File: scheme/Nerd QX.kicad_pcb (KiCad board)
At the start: 6 copper layers, 89 x 184 mm, 263 parts, among them J1 Connector 02x01, J2 Conn_01x04, M1 Fan_4pin, M2 Fan_4pin, M3 Fan_4pin, U10 CSD95472Q5MC, U19 BM1370_mode1, U2 TMUX1109RSVR, U20 BM1370_mode1, U25 BM1370_mode1, U26 BM1370_mode1, U3 TPS53647, U30 T-Display-S3, U32 EMC2302-1, U33 TXU0102-DCU, U35 TXU0304PW, U36 MCP1824T-1202E, U37 TMP1075, U38 TMP1075, U4 CSD95472Q5MC, U5 TMP451, U6 AP3211, U7 MCP1824T-0802E, U8 25MHz, U9 CSD95472Q5MC

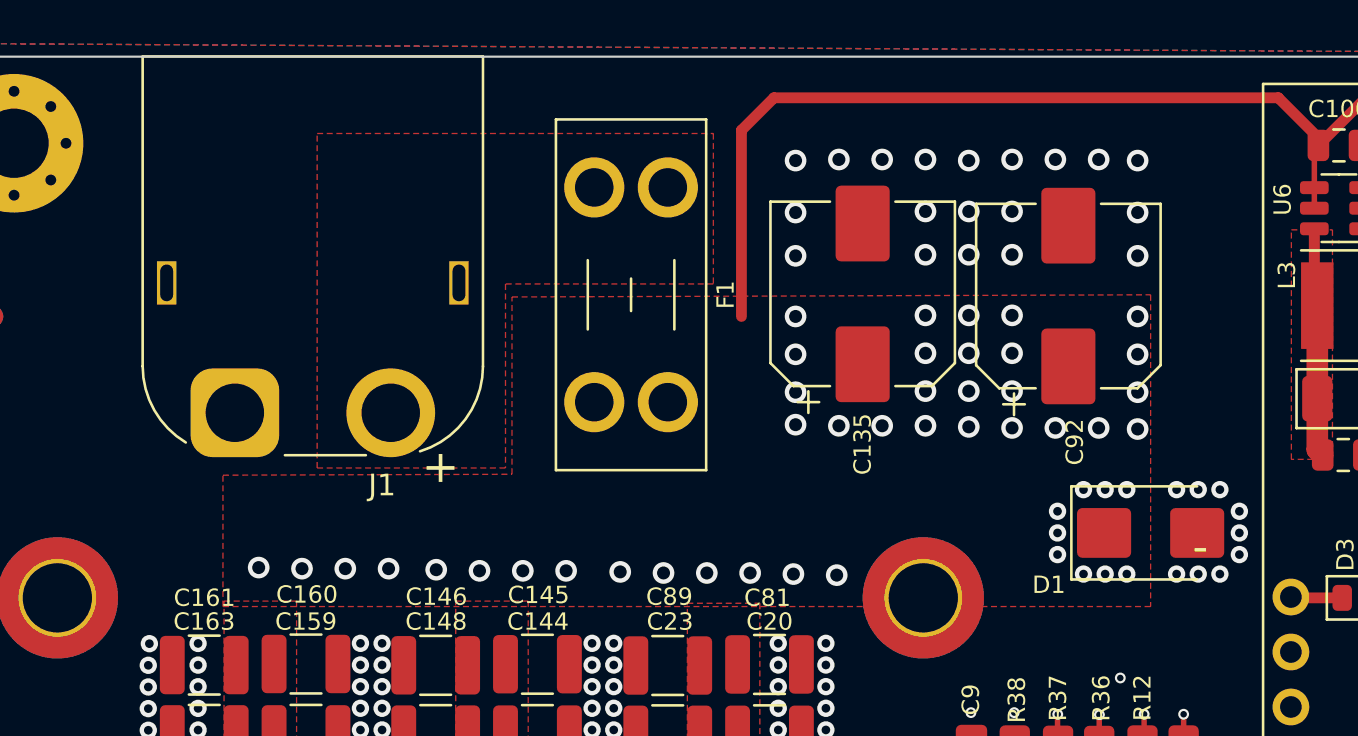
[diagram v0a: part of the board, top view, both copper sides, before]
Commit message: Moved J1 XT60 connector from top to bottom side of the board. Exported new gerber files, drill files and P&P files. Exported new PCB STEP file.
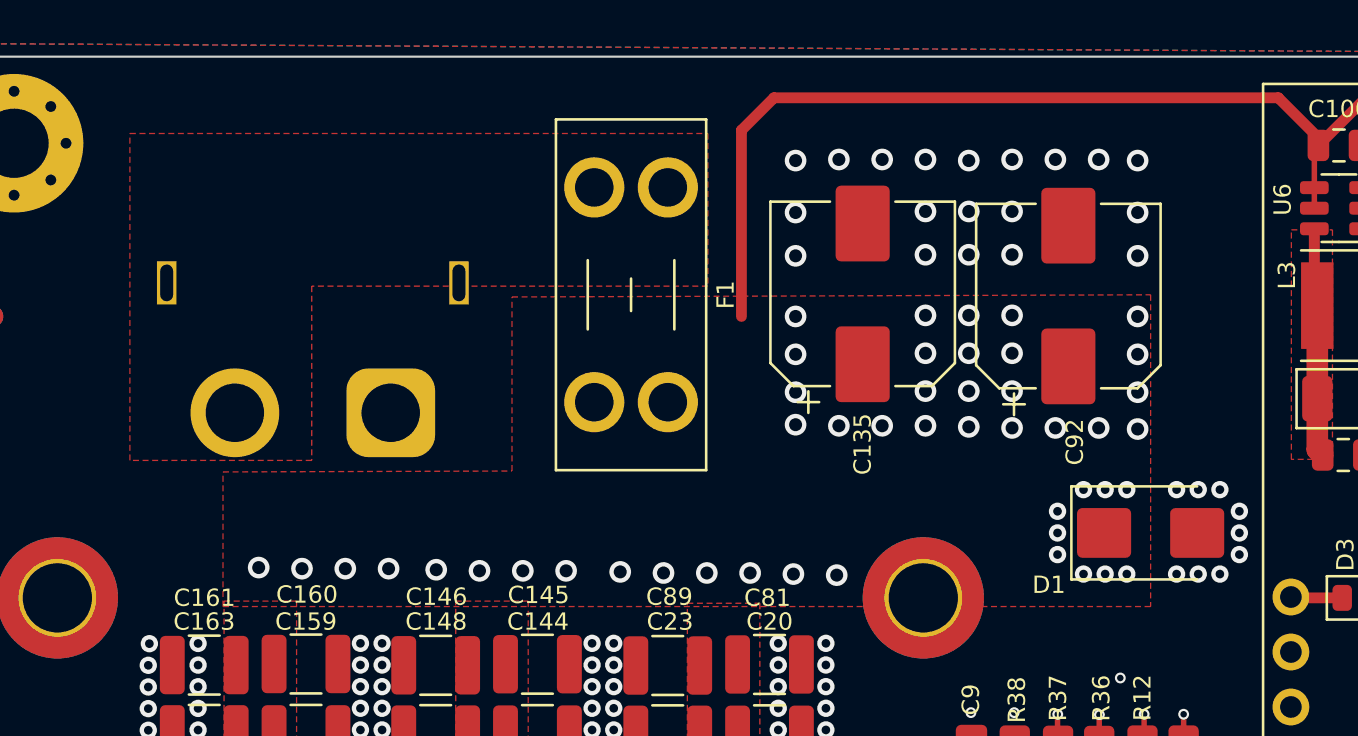
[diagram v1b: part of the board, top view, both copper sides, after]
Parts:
- J1: moved to B.Cu
- moved J1 7.20 mm to (70.4, 29.4), turned to 180 degrees
